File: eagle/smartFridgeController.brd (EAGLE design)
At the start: 77.8 x 54 mm, 7 parts

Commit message: might work
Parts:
- removed CPC1709: (no value), SparkFun-Connectors:1X05
- added CPC1706: S102S02, relay:S202S02
- moved OKI-78SR-5/1.5-W36-C 41.1 mm to (11.4, 24.1)
- moved C2 37.0 mm to (21.6, 38.1)
- moved R6 25.4 mm to (20.3, 29.2), turned to 90 degrees
- moved R5 25.0 mm to (24.1, 26.7), turned to 270 degrees
- moved JST 1.80 mm to (16.5, 33.0), turned to 90 degrees
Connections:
- net +VE: now also CPC1706.1, JST.1; no longer CPC1709.4
- net -VE: now also CPC1706.2, JST.2; no longer CPC1709.5
- net D8_RELAY_PIN: now also CPC1706.4; no longer CPC1709.1
- net GND: now also CPC1706.3; no longer CPC1709.2
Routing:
- net VIN: track 0.00 -> 49.5 mm
- net D8_RELAY_PIN: track 0.00 -> 42.6 mm
- net -VE: track 0.00 -> 35.7 mm
- net +VE: track 0.00 -> 33.0 mm
- net A0_VCC_VD: track 0.00 -> 32.3 mm
- net VCC: track 0.00 -> 18.7 mm
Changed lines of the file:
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@@
 </autorouter>
 <elements>
-<element name="C2" library="SparkFun-Capacitors" package="CAP-PTH-SMALL-KIT" value="0.1U" x="7.62" y="3.81">
-<attribute name="PROD_ID" value="CAP-08370" x="-3.81" y="30.48" size="1.778" layer="27" display="off"/>
+<element name="C2" library="SparkFun-Capacitors" package="CAP-PTH-SMALL-KIT" value="0.1U" x="21.59" y="38.1">
+<attribute name="PROD_ID" value="CAP-08370" x="10.16" y="64.77" size="1.778" layer="27" display="off"/>
 </element>
-<element name="R5" library="SparkFun-Resistors" package="AXIAL-0.3" value="3.3M" x="34.29" y="3.81">
-<attribute name="PROD_ID" value="RES-12182" x="34.29" y="26.67" size="1.778" layer="27" display="off"/>
+<element name="R5" library="SparkFun-Resistors" package="AXIAL-0.3" value="3.3M" x="24.13" y="26.67" rot="R270">
+<attribute name="PROD_ID" value="RES-12182" x="46.99" y="26.67" size="1.778" layer="27" rot="R270" display="off"/>
 </element>
-<element name="JST" library="SparkFun-Connectors" package="JST-4-PTH" value="" x="17.78" y="31.75">
-<attribute name="PROD_ID" value="WIRE-13531" x="17.78" y="3.81" size="1.778" layer="27" display="off"/>
-<attribute name="SF_ID" value="PRT-09916" x="17.78" y="3.81" size="1.778" layer="27" display="off"/>
+<element name="JST" library="SparkFun-Connectors" package="JST-4-PTH" value="" x="16.51" y="33.02" rot="R90">
+<attribute name="PROD_ID" value="WIRE-13531" x="44.45" y="33.02" size="1.778" layer="27" rot="R90" display="off"/>
+<attribute name="SF_ID" value="PRT-09916" x="44.45" y="33.02" size="1.778" layer="27" rot="R90" display="off"/>
 </element>
-<element name="R6" library="adafruit" package="0309/12" value="27M" x="21.59" y="3.81"/>
+<element name="R6" library="adafruit" package="0309/12" value="27M" x="20.32" y="29.21" rot="R90"/>
 <element name="U$1" library="Moteino" package="MOTEINO_R6" value="MOTEINOR6" x="41.91" y="19.05" rot="MR0"/>
-<element name="OKI-78SR-5/1.5-W36-C" library="SparkFun-Connectors" package="1X03" value="Regulator" x="52.07" y="17.78">
-<attribute name="PROD_ID" value="XXX-00000" x="52.07" y="17.78" size="1.778" layer="27" display="off"/>
+<element name="OKI-78SR-5/1.5-W36-C" library="SparkFun-Connectors" package="1X03" value="Regulator" x="11.43" y="24.13">
+<attribute name="PROD_ID" value="XXX-00000" x="11.43" y="24.13" size="1.778" layer="27" display="off"/>
 </element>
-<element name="CPC1709" library="SparkFun-Connectors" package="1X05" value="" x="6.35" y="-16.51"/>
+<element name="CPC1706" library="relay" library_urn="urn:adsk.eagle:library:339" package="S202S02" package3d_urn="urn:adsk.eagle:package:24541/1" value="S102S02" x="45.72" y="30.48" rot="R90">
+<attribute name="MF" value="" x="45.72" y="30.48" size="1.778" layer="27" rot="R90" display="off"/>
+<attribute name="MPN" value="" x="45.72" y="30.48" size="1.778" layer="27" rot="R90" display="off"/>
+<attribute name="OC_FARNELL" value="unknown" x="45.72" y="30.48" size="1.778" layer="27" rot="R90" display="off"/>
+<attribute name="OC_NEWARK" value="unknown" x="45.72" y="30.48" size="1.778" layer="27" rot="R90" display="off"/>
+</element>
 </elements>
 <signals>
@@
 <contactref element="JST" pad="3"/>
 <contactref element="OKI-78SR-5/1.5-W36-C" pad="3"/>
-<contactref element="CPC1709" pad="2"/>
-<wire x1="30.48" y1="3.81" x2="57.15" y2="17.78" width="0" layer="19" extent="1-1"/>
-<wire x1="9.017" y1="3.81" x2="30.48" y2="3.81" width="0" layer="19" extent="1-1"/>
-<wire x1="8.89" y1="-16.51" x2="9.017" y2="3.81" width="0" layer="19" extent="1-1"/>
-<wire x1="18.78" y1="31.75" x2="9.017" y2="3.81" width="0" layer="19" extent="1-1"/>
+<contactref element="CPC1706" pad="3"/>
 </signal>
 <signal name="VIN" class="1">
 <contactref element="U$1" pad="VIN"/>
 <contactref element="OKI-78SR-5/1.5-W36-C" pad="2"/>
-<wire x1="38.1" y1="40.64" x2="54.61" y2="17.78" width="0" layer="19" extent="1-1"/>
+<wire x1="37.592" y1="40.64" x2="38.1" y2="40.64" width="0.6096" layer="1"/>
+<wire x1="36.195" y1="42.037" x2="37.592" y2="40.64" width="0.6096" layer="1"/>
+<wire x1="9.525" y1="42.037" x2="36.195" y2="42.037" width="0.6096" layer="1"/>
+<wire x1="8.763" y1="41.275" x2="9.525" y2="42.037" width="0.6096" layer="1"/>
+<wire x1="8.763" y1="35.941" x2="8.763" y2="41.275" width="0.6096" layer="1"/>
+<wire x1="13.97" y1="30.734" x2="8.763" y2="35.941" width="0.6096" layer="1"/>
+<wire x1="13.97" y1="24.13" x2="13.97" y2="30.734" width="0.6096" layer="1"/>
 </signal>
 <signal name="VCC" class="1">
@@
 <contactref element="R6" pad="2"/>
 <contactref element="OKI-78SR-5/1.5-W36-C" pad="1"/>
-<wire x1="27.94" y1="3.81" x2="52.07" y2="17.78" width="0" layer="19" extent="1-1"/>
-<wire x1="20.78" y1="31.75" x2="27.94" y2="3.81" width="0" layer="19" extent="1-1"/>
+<wire x1="19.939" y1="35.941" x2="16.51" y2="35.941" width="0.6096" layer="1"/>
+<wire x1="20.32" y1="35.56" x2="19.939" y2="35.941" width="0.6096" layer="1"/>
+<wire x1="16.51" y1="35.941" x2="16.51" y2="36.02" width="0.6096" layer="1"/>
+<wire x1="11.43" y1="25.019" x2="11.43" y2="24.13" width="0.6096" layer="16"/>
+<wire x1="14.351" y1="27.94" x2="11.43" y2="25.019" width="0.6096" layer="16"/>
+<wire x1="14.351" y1="34.798" x2="14.351" y2="27.94" width="0.6096" layer="16"/>
+<wire x1="15.621" y1="36.068" x2="14.351" y2="34.798" width="0.6096" layer="16"/>
+<wire x1="16.51" y1="36.068" x2="15.621" y2="36.068" width="0.6096" layer="16"/>
+<wire x1="16.51" y1="36.068" x2="16.51" y2="36.02" width="0.6096" layer="16"/>
 </signal>
-<signal name="A0_VCC_VD">
+<signal name="A0_VCC_VD" class="1">
 <contactref element="U$1" pad="A0"/>
 <contactref element="C2" pad="1"/>
 <contactref element="R5" pad="P$2"/>
 <contactref element="R6" pad="1"/>
-<wire x1="6.223" y1="3.81" x2="10.16" y2="40.64" width="0" layer="19" extent="1-1"/>
-<wire x1="38.1" y1="3.81" x2="6.223" y2="3.81" width="0" layer="19" extent="1-1"/>
-<wire x1="15.24" y1="3.81" x2="38.1" y2="3.81" width="0" layer="19" extent="1-1"/>
+<wire x1="24.13" y1="22.86" x2="20.32" y2="22.86" width="0.6096" layer="1"/>
+<wire x1="10.668" y1="40.64" x2="10.16" y2="40.64" width="0.6096" layer="1"/>
+<wire x1="13.208" y1="38.1" x2="10.668" y2="40.64" width="0.6096" layer="1"/>
+<wire x1="20.193" y1="38.1" x2="15.113" y2="38.1" width="0.6096" layer="1"/>
+<wire x1="15.113" y1="38.1" x2="13.208" y2="38.1" width="0.6096" layer="1"/>
+<wire x1="20.193" y1="24.384" x2="20.193" y2="23.114" width="0.6096" layer="1"/>
+<wire x1="15.113" y1="29.464" x2="20.193" y2="24.384" width="0.6096" layer="1"/>
+<wire x1="15.113" y1="38.1" x2="15.113" y2="29.464" width="0.6096" layer="1"/>
+<wire x1="20.193" y1="23.114" x2="20.32" y2="22.86" width="0.6096" layer="1"/>
 </signal>
-<signal name="D8_RELAY_PIN">
-<contactref element="CPC1709" pad="1"/>
+<signal name="D8_RELAY_PIN" class="1">
 <contactref element="U$1" pad="D8"/>
-<wire x1="6.35" y1="-16.51" x2="22.86" y2="20.32" width="0" layer="19" extent="1-1"/>
+<contactref element="CPC1706" pad="4"/>
+<wire x1="45.72" y1="37.465" x2="45.72" y2="38.1" width="0.6096" layer="1"/>
+<wire x1="47.117" y1="36.068" x2="45.72" y2="37.465" width="0.6096" layer="1"/>
+<wire x1="47.117" y1="22.352" x2="47.117" y2="36.068" width="0.6096" layer="1"/>
+<wire x1="43.688" y1="18.923" x2="47.117" y2="22.352" width="0.6096" layer="1"/>
+<wire x1="24.257" y1="18.923" x2="43.688" y2="18.923" width="0.6096" layer="1"/>
+<wire x1="22.86" y1="20.32" x2="24.257" y2="18.923" width="0.6096" layer="1"/>
 </signal>
-<signal name="+VE">
-<contactref element="CPC1709" pad="4"/>
+<signal name="+VE" class="1">
+<contactref element="JST" pad="1"/>
+<contactref element="CPC1706" pad="1"/>
+<wire x1="42.672" y1="22.86" x2="45.72" y2="22.86" width="0.6096" layer="1"/>
+<wire x1="41.656" y1="21.844" x2="42.672" y2="22.86" width="0.6096" layer="1"/>
+<wire x1="27.305" y1="21.844" x2="41.656" y2="21.844" width="0.6096" layer="1"/>
+<wire x1="19.177" y1="29.972" x2="27.305" y2="21.844" width="0.6096" layer="1"/>
+<wire x1="16.51" y1="29.972" x2="19.177" y2="29.972" width="0.6096" layer="1"/>
+<wire x1="16.51" y1="29.972" x2="16.51" y2="30.02" width="0.6096" layer="1"/>
 </signal>
-<signal name="-VE">
-<contactref element="CPC1709" pad="5"/>
+<signal name="-VE" class="1">
+<contactref element="JST" pad="2"/>
+<contactref element="CPC1706" pad="2"/>
+<wire x1="45.72" y1="27.178" x2="45.72" y2="27.94" width="0.6096" layer="1"/>
+<wire x1="41.275" y1="22.733" x2="45.72" y2="27.178" width="0.6096" layer="1"/>
+<wire x1="27.686" y1="22.733" x2="41.275" y2="22.733" width="0.6096" layer="1"/>
+<wire x1="18.415" y1="32.004" x2="27.686" y2="22.733" width="0.6096" layer="1"/>
+<wire x1="16.51" y1="32.004" x2="18.415" y2="32.004" width="0.6096" layer="1"/>
+<wire x1="16.51" y1="32.004" x2="16.51" y2="32.02" width="0.6096" layer="1"/>
 </signal>
 </signals>
@@
 which will not be processed correctly with this version.
 </note>
+<note version="8.2" severity="warning">
+Since Version 8.2, EAGLE supports online libraries. The ids
+of those online libraries will not be understood (or retained)
+with this version.
+</note>
+<note version="8.3" severity="warning">
+Since Version 8.3, EAGLE supports URNs for individual library
+assets (packages, symbols, and devices). The URNs of those assets
+will not be understood (or retained) with this version.
+</note>
+<note version="8.3" severity="warning">
+Since Version 8.3, EAGLE supports the association of 3D packages
+with devices in libraries, schematics, and board files. Those 3D
+packages will not be understood (or retained) with this version.
+</note>
 </compatibility>

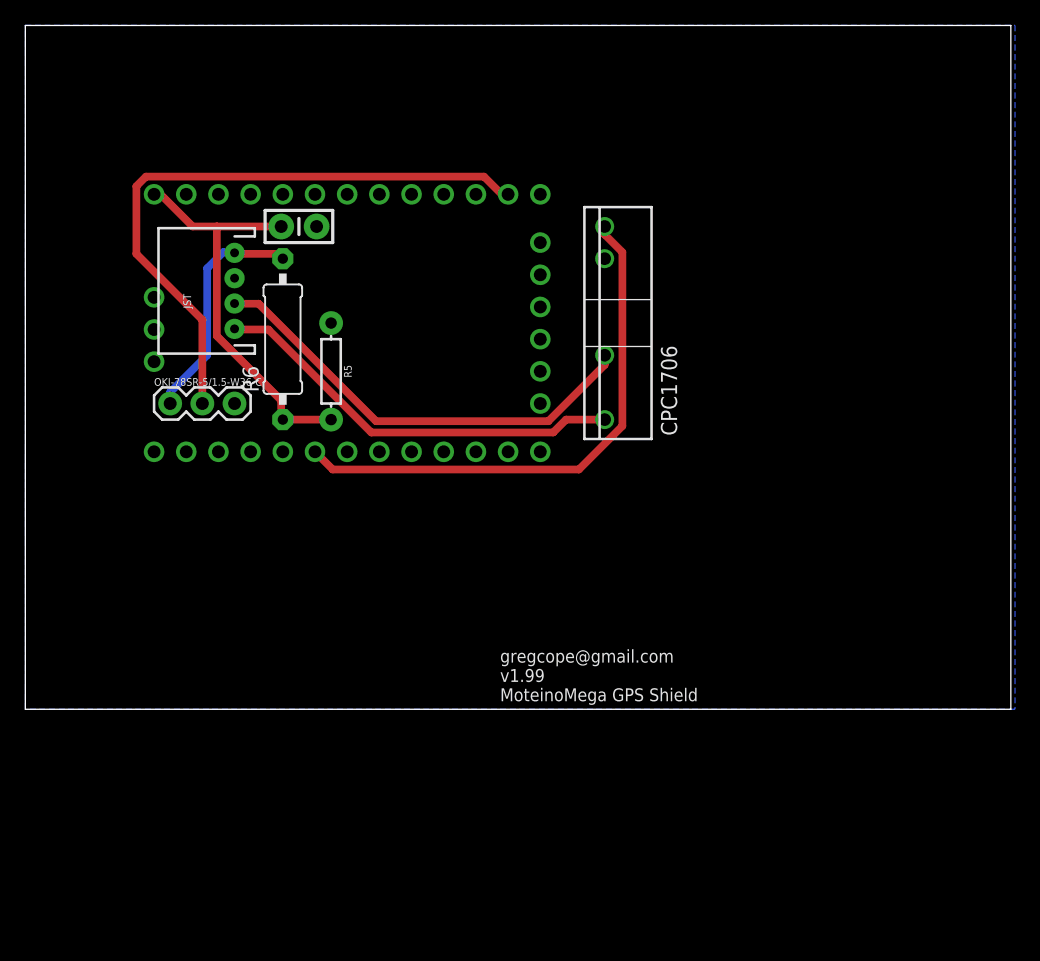
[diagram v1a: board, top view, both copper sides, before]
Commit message: Added DS header
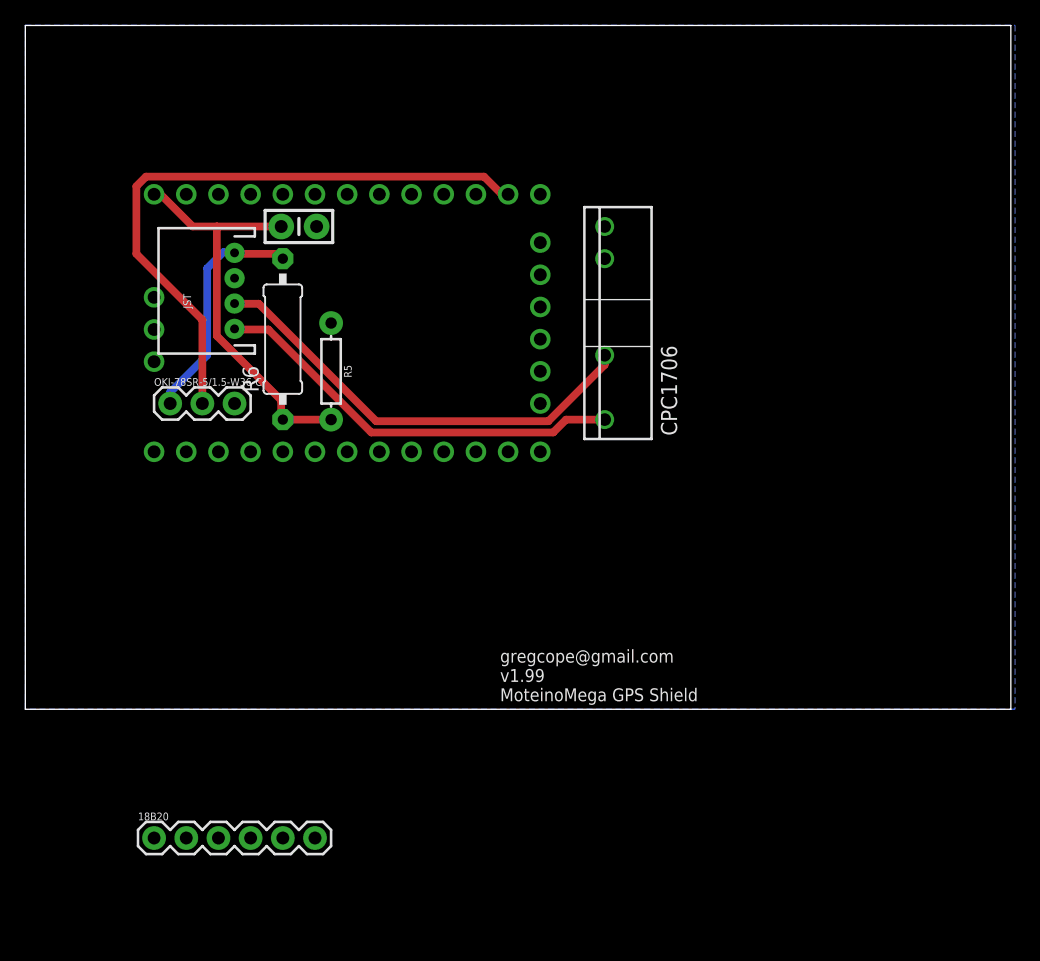
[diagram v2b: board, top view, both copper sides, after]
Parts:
- added 18B20: (no value), SparkFun-Connectors:1X06
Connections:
- removed net D8_RELAY_PIN: CPC1706.4, U$1.D8
- new net D15_RELAY_PIN: CPC1706.4, U$1.A1
- new net D4_DS2_DATA: 18B20.6, U$1.D4
- new net D5_DS2_PWR: 18B20.5, U$1.D5
- new net D6_DS1_DATA: 18B20.3, U$1.D6
- new net D7_DS1_PWR: 18B20.2, U$1.D7
- new net N$11: U$1.A2
- net GND: now also 18B20.1, 18B20.4
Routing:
- net D8_RELAY_PIN: track 42.6 -> 0.00 mm
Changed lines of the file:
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@@
 <attribute name="OC_NEWARK" value="unknown" x="45.72" y="30.48" size="1.778" layer="27" rot="R90" display="off"/>
+</element>
+<element name="18B20" library="SparkFun-Connectors" package="1X06" value="" x="10.16" y="-10.16">
+<attribute name="PROD_ID" value="CONN-08437" x="10.16" y="-10.16" size="1.778" layer="27" display="off"/>
 </element>
 </elements>
@@
 <contactref element="OKI-78SR-5/1.5-W36-C" pad="3"/>
 <contactref element="CPC1706" pad="3"/>
+<contactref element="18B20" pad="4"/>
+<contactref element="18B20" pad="1"/>
+<wire x1="24.13" y1="30.48" x2="45.72" y2="35.56" width="0" layer="19" extent="1-1"/>
+<wire x1="22.987" y1="38.1" x2="24.13" y2="30.48" width="0" layer="19" extent="1-1"/>
+<wire x1="16.51" y1="34.02" x2="22.987" y2="38.1" width="0" layer="19" extent="1-1"/>
+<wire x1="16.51" y1="24.13" x2="16.51" y2="34.02" width="0" layer="19" extent="1-1"/>
+<wire x1="17.78" y1="-10.16" x2="16.51" y2="24.13" width="0" layer="19" extent="1-1"/>
+<wire x1="10.16" y1="-10.16" x2="17.78" y2="-10.16" width="0" layer="19" extent="1-1"/>
 </signal>
 <signal name="VIN" class="1">
@@
 <wire x1="20.193" y1="23.114" x2="20.32" y2="22.86" width="0.6096" layer="1"/>
 </signal>
-<signal name="D8_RELAY_PIN" class="1">
-<contactref element="U$1" pad="D8"/>
-<contactref element="CPC1706" pad="4"/>
-<wire x1="45.72" y1="37.465" x2="45.72" y2="38.1" width="0.6096" layer="1"/>
-<wire x1="47.117" y1="36.068" x2="45.72" y2="37.465" width="0.6096" layer="1"/>
-<wire x1="47.117" y1="22.352" x2="47.117" y2="36.068" width="0.6096" layer="1"/>
-<wire x1="43.688" y1="18.923" x2="47.117" y2="22.352" width="0.6096" layer="1"/>
-<wire x1="24.257" y1="18.923" x2="43.688" y2="18.923" width="0.6096" layer="1"/>
-<wire x1="22.86" y1="20.32" x2="24.257" y2="18.923" width="0.6096" layer="1"/>
-</signal>
 <signal name="+VE" class="1">
 <contactref element="JST" pad="1"/>
@@
 <wire x1="16.51" y1="32.004" x2="16.51" y2="32.02" width="0.6096" layer="1"/>
 </signal>
+<signal name="D7_DS1_PWR">
+<contactref element="U$1" pad="D7"/>
+<contactref element="18B20" pad="2"/>
+<wire x1="12.7" y1="-10.16" x2="25.4" y2="20.32" width="0" layer="19" extent="1-1"/>
+</signal>
+<signal name="D6_DS1_DATA">
+<contactref element="U$1" pad="D6"/>
+<contactref element="18B20" pad="3"/>
+<wire x1="15.24" y1="-10.16" x2="27.94" y2="20.32" width="0" layer="19" extent="1-1"/>
+</signal>
+<signal name="D4_DS2_DATA">
+<contactref element="U$1" pad="D4"/>
+<contactref element="18B20" pad="6"/>
+<wire x1="22.86" y1="-10.16" x2="33.02" y2="20.32" width="0" layer="19" extent="1-1"/>
+</signal>
+<signal name="D15_RELAY_PIN">
+<contactref element="U$1" pad="A1"/>
+<contactref element="CPC1706" pad="4"/>
+<wire x1="12.7" y1="40.64" x2="45.72" y2="38.1" width="0" layer="19" extent="1-1"/>
+</signal>
+<signal name="N$11">
+<contactref element="U$1" pad="A2"/>
+</signal>
+<signal name="D5_DS2_PWR">
+<contactref element="U$1" pad="D5"/>
+<contactref element="18B20" pad="5"/>
+<wire x1="20.32" y1="-10.16" x2="30.48" y2="20.32" width="0" layer="19" extent="1-1"/>
+</signal>
 </signals>

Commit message: Board layed out
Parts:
- moved CPC1706 20.5 mm to (35.6, 12.7)
- moved C2 19.9 mm to (12.7, 20.3)
- moved JST 19.9 mm to (7.62, 15.2)
- moved OKI-78SR-5/1.5-W36-C 19.9 mm to (2.54, 6.35)
- moved R5 19.9 mm to (15.2, 8.89)
- moved R6 19.9 mm to (11.4, 11.4)
- moved U$1 19.9 mm to (33.0, 1.27)
- moved 18B20 18.8 mm to (19.1, 6.35), turned to 90 degrees
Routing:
- net D15_RELAY_PIN: track 0.00 -> 34.2 mm
- net D4_DS2_DATA: track 0.00 -> 18.6 mm
- net VIN: track 49.5 -> 33.5 mm
- net D5_DS2_PWR: track 0.00 -> 15.0 mm
- net D6_DS1_DATA: track 0.00 -> 10.0 mm
- net D7_DS1_PWR: track 0.00 -> 7.40 mm
- net +VE: track 33.0 -> 40.4 mm
- net -VE: track 35.7 -> 39.8 mm
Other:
- board size 77.8 x 54 mm -> 39.7 x 24.8 mm
- board text added: "gregcope@gmail.com v0.1 smartFridgeController"
- board text removed: "gregcope@gmail.com v1.99 MoteinoMega GPS Shield"

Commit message: extended board
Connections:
- removed net N$11: U$1.A2
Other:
- board size 39.7 x 24.8 mm -> 39.7 x 25.4 mm
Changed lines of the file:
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@@
 <setting verticaltext="up"/>
 </settings>
-<grid distance="0.05" unitdist="inch" unit="inch" style="lines" multiple="1" display="no" altdistance="0.025" altunitdist="inch" altunit="inch"/>
+<grid distance="0.05" unitdist="inch" unit="inch" style="dots" multiple="1" display="yes" altdistance="0.025" altunitdist="inch" altunit="inch"/>
 <layers>
 <layer number="1" name="Top" color="4" fill="1" visible="yes" active="yes"/>
@@
 <plain>
 <wire x1="0" y1="0" x2="39.675" y2="0" width="0" layer="20"/>
-<wire x1="39.675" y1="0" x2="39.675" y2="24.755" width="0" layer="20"/>
-<wire x1="39.675" y1="24.755" x2="0" y2="24.755" width="0" layer="20"/>
-<wire x1="0" y1="24.755" x2="0" y2="0" width="0" layer="20"/>
+<wire x1="39.675" y1="0" x2="39.675" y2="25.39" width="0" layer="20"/>
+<wire x1="39.675" y1="25.39" x2="0" y2="25.39" width="0" layer="20"/>
+<wire x1="0" y1="25.39" x2="0" y2="0" width="0" layer="20"/>
 <text x="26.035" y="4.445" size="1.016" layer="25" font="vector" rot="R90">gregcope@gmail.com
 v0.1
@@
 <signal name="GND" class="1">
 <polygon width="0.4064" layer="16" isolate="0.3048">
-<vertex x="0" y="24.765"/>
-<vertex x="40.005" y="24.765"/>
+<vertex x="0" y="25.4"/>
+<vertex x="39.37" y="25.4"/>
 <vertex x="40.005" y="0"/>
 <vertex x="0" y="0"/>
@@
 <wire x1="3.81" y1="22.86" x2="5.08" y2="24.13" width="0.254" layer="1"/>
 </signal>
-<signal name="N$11">
-<contactref element="U$1" pad="A2"/>
-</signal>
 <signal name="D5_DS2_PWR">
 <contactref element="U$1" pad="D5"/>
@@
 </signal>
 </signals>
+<errors>
+</errors>
 </board>
 </drawing>
